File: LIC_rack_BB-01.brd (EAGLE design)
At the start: 162 x 102 mm, 25 parts, among them IC1 74HC125D, IC3 74HC125D, IC4 MEGA128-A, IC6 MAX481CSA, Q1 14.7456, Q2 IRLL014, U1 ATPROG-V

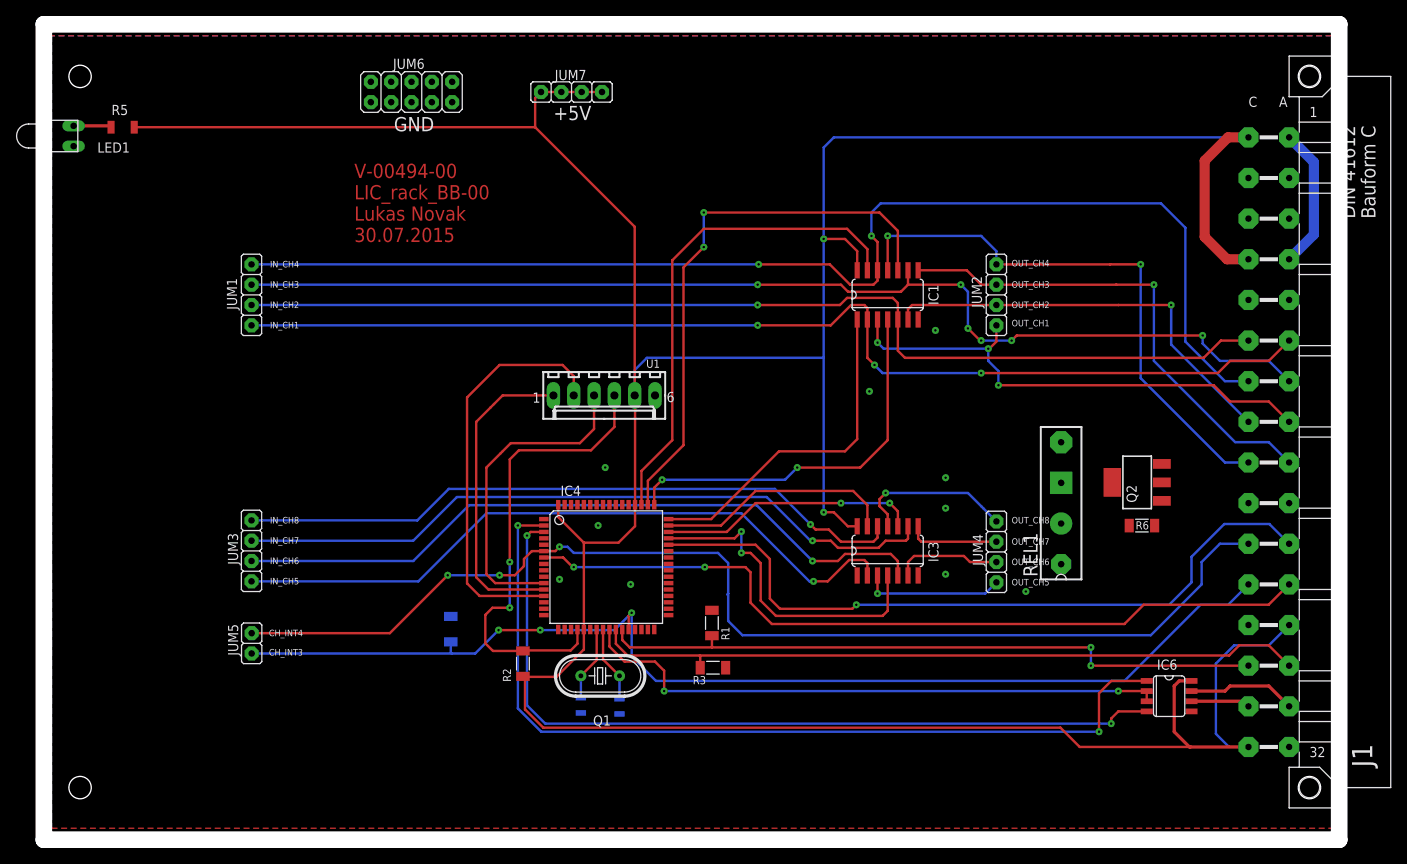
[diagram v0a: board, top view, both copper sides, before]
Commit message: Pridána nová verze
Přidána nová verze zkráceno na 4 In a 4 Out a přidáno relé na desku
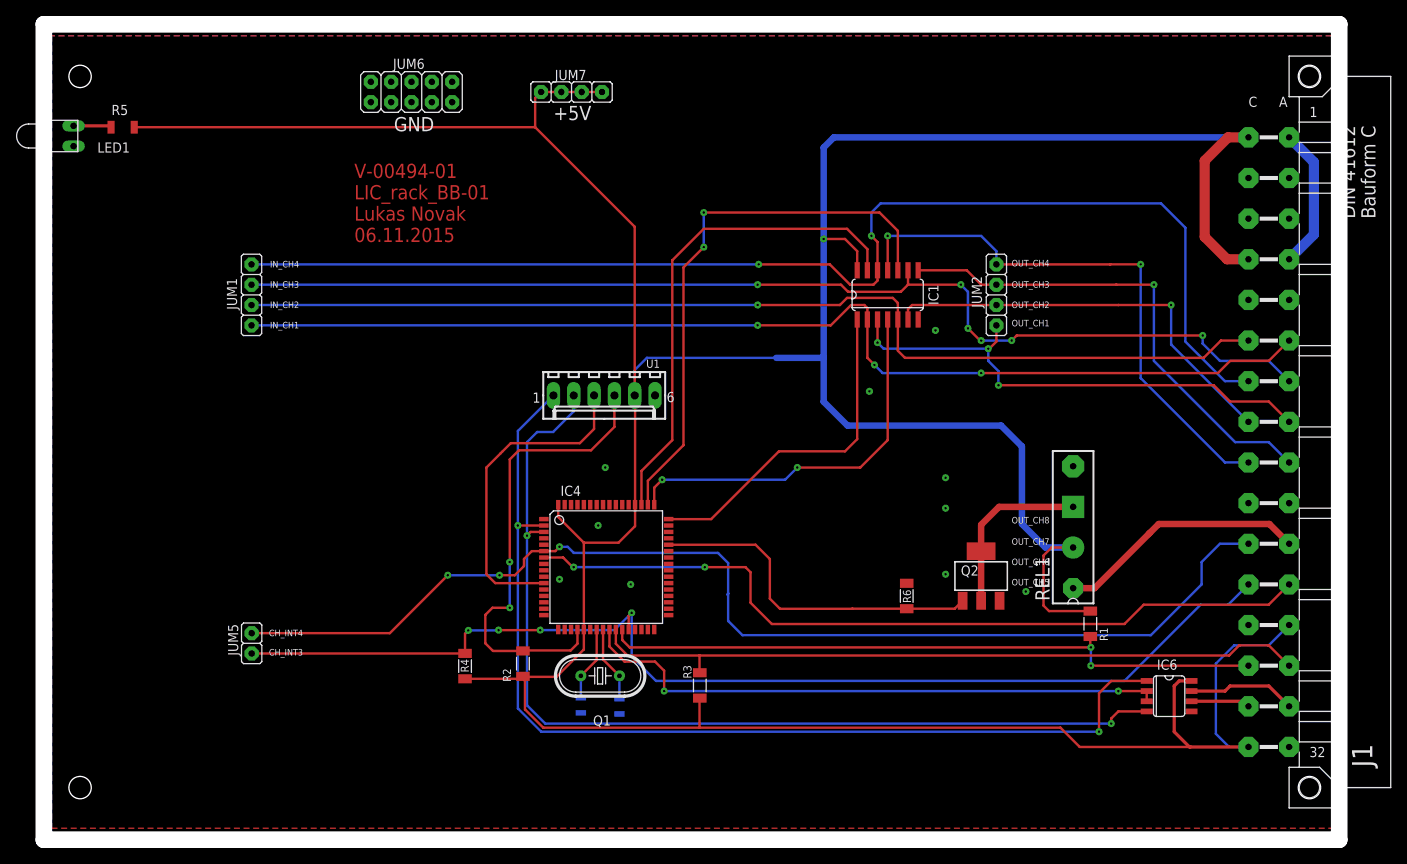
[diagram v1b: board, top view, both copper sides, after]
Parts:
- removed IC3: 74HC125D, 74xx-eu:SO14
- removed JUM3, JUM4: S1G4_JUMP, #PaJa_konektory:S1G4_JUM
- R6: value (none) -> 10k
- moved R1 47.3 mm to (129.8, -24.0)
- moved R6 30.7 mm to (106.9, -20.5), turned to 270 degrees
- moved Q2 22.7 mm to (116.2, -18.0), turned to 0 degrees
- moved R4 4.95 mm to (51.7, -29.3), flipped to the top, turned to 90 degrees
- moved REL1 3.35 mm to (127.7, -11.9)
- moved R3 2.76 mm to (81.0, -31.7), turned to 90 degrees
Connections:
- removed net IN_CH5: IC3.2, JUM3.4
- removed net IN_CH6: IC3.5, JUM3.3
- removed net IN_CH7: IC3.9, JUM3.2
- removed net IN_CH8: IC3.12, JUM3.1
- removed net IN_LASER: REL1.1
- removed net OUT_CH5: IC3.3, JUM4.4
- removed net OUT_CH6: IC3.6, JUM4.3
- removed net OUT_CH7: IC3.8, JUM4.2
- removed net OUT_CH8: IC3.11, JUM4.1
- removed net PA7: Q2.1, R6.2
- new net OUT_LASER: J1.A22, REL1.1
- net +5V: now also R1.1, R3.1, R4.1; no longer IC3.14
- net GND: no longer IC3.7, R1.1, R3.1, R4.1
- net PX_CH5: now also Q2.1, R6.2; no longer IC3.1, J1.A22
- net PX_CH6: no longer IC3.4
- net PX_CH7: no longer IC3.10
- net PX_CH8: no longer IC3.13
- net PX_MISO: no longer U1.2
- net PX_MOSI: no longer U1.1
- net SYS_RX: now also U1.1
- net SYS_TX: now also U1.2
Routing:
- net IN_CH6: track 89.1 -> 0.00 mm, vias 1 -> 0
- net IN_CH7: track 89.0 -> 0.00 mm, vias 1 -> 0
- net IN_CH5: track 86.8 -> 0.00 mm, vias 1 -> 0
- net IN_CH8: track 84.3 -> 0.00 mm, vias 1 -> 0
- net +5V: track 446.8 -> 500.3 mm, vias 2 -> 1
- net PX_MISO: track 51.5 -> 0.00 mm
- net PX_CH5: track 91.1 -> 43.4 mm, vias 1 -> 0
- net PX_CH6: track 41.1 -> 0.00 mm, vias 2 -> 0
- net PX_MOSI: track 39.5 -> 0.00 mm
- net PX_CH7: track 32.4 -> 0.00 mm, vias 2 -> 0
- net OUT_LASER: track 0.00 -> 31.3 mm
- net PX_CH8: track 30.0 -> 0.00 mm
- net N$3: track 0.00 -> 21.9 mm
- net SYS_TX: track 102.9 -> 124.0 mm
- net OUT_CH8: track 20.2 -> 0.00 mm, vias 1 -> 0
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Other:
- board text added: "V-00494-01 LIC_rack_BB-01 Lukas Novak 06.11.2015"
- board text removed: "IN_CH5"
- board text removed: "IN_CH6"
- board text removed: "IN_CH7"
- board text removed: "IN_CH8"
- board text removed: "V-00494-00 LIC_rack_BB-00 Lukas Novak 30.07.2015"
